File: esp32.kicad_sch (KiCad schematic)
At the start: 22 parts, among them IC1 ESP32-S3-MINI-1U-N8, IC2 CP2102N-A02-GQFN24, J4 USB_C_Receptacle_USB2.0, Q6 NPN, Q7 NPN, SW3 SW_Push, U15 USBLC6-2SC6

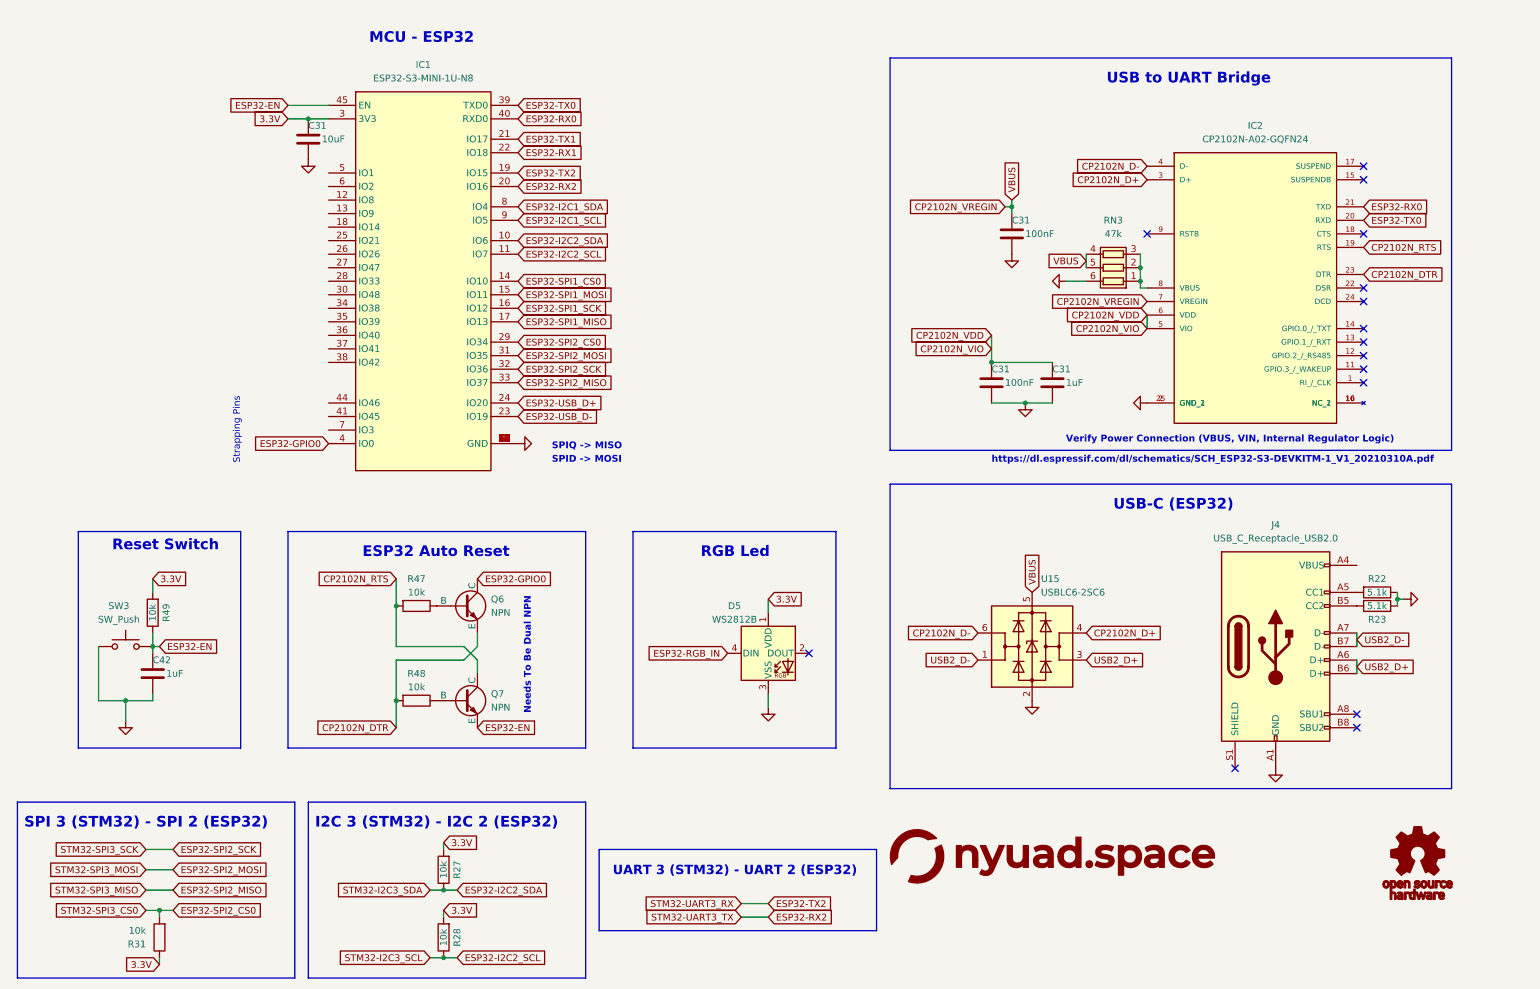
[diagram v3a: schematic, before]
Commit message: Added INA219
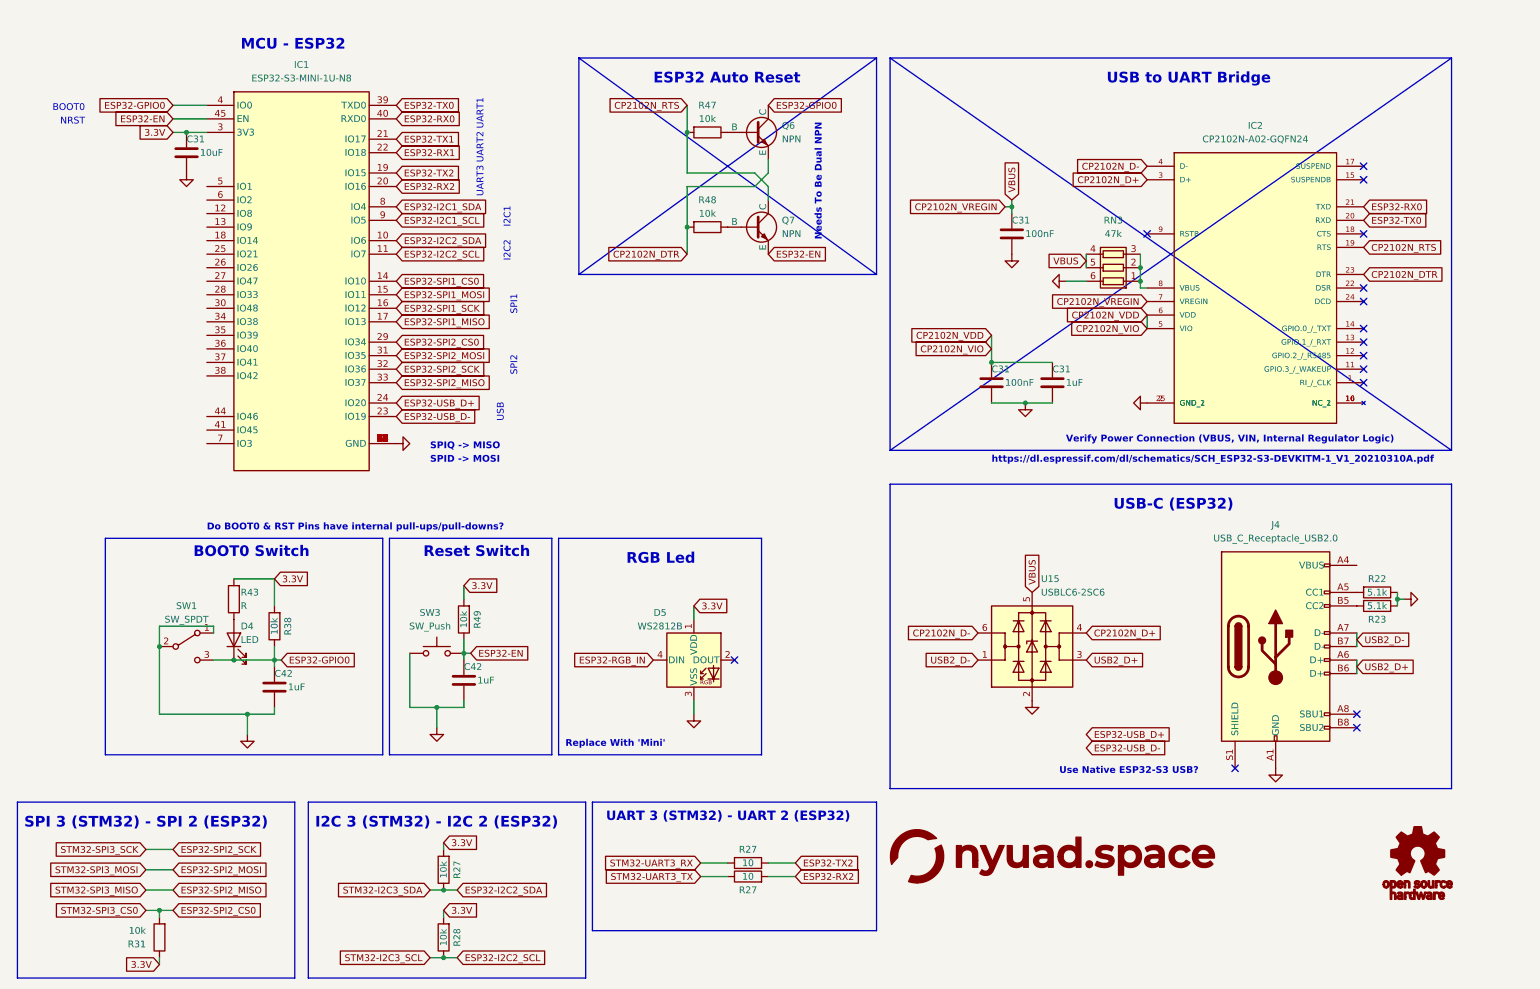
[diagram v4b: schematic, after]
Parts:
- added C42: 1uF, Capacitor_SMD:C_0201_0603Metric, symbol Device:C
- added D4: LED, symbol Device:LED
- added R27 (x2): 10, Resistor_SMD:R_0201_0603Metric, symbol Device:R
- added R38: 10k, symbol Device:R
- added R43: R, symbol Device:R
- added SW1: SW_SPDT, symbol Switch:SW_SPDT
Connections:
- net 3.3V: now also R38.2, R43.2
- net ESP32-GPIO0: now also C42.1, D4.1 (K), R38.1, SW1.3 (C)
- net ESP32-RX2: now also R27.2
- net ESP32-TX2: now also R27.2
- net GND: now also C42.2, SW1.1 (A), SW1.2 (B)
- new net: D4.2 (A), R43.1
- new net STM32-UART3_RX: R27.1
- new net STM32-UART3_TX: R27.1
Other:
- note added: "BOOT0"
- note added: "BOOT0 Switch"
- note added: "Do BOOT0 & RST Pins have internal pull-ups/pull-downs?"
- note added: "I2C1"
- note added: "I2C2"
- note added: "NRST"
- note added: "Replace With 'Mini'"
- note added: "SPI1"
- note added: "SPI2"
- note added: "UART1"
- note added: "UART2"
- note added: "UART3"
- note added: "USB"
- note added: "Use Native ESP32-S3 USB?"
- note removed: "Strapping Pins"
- moved on the sheet: C31, C42, D5, IC1, Q6, Q7, R47, R48, R49, SW3

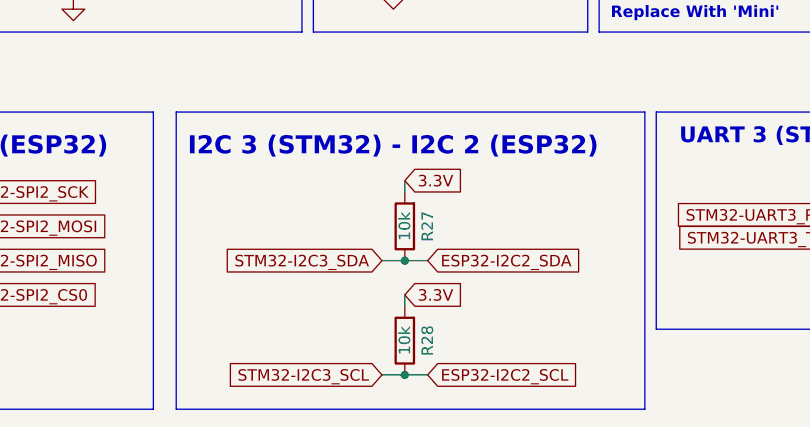
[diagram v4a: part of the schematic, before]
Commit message: Added connectors
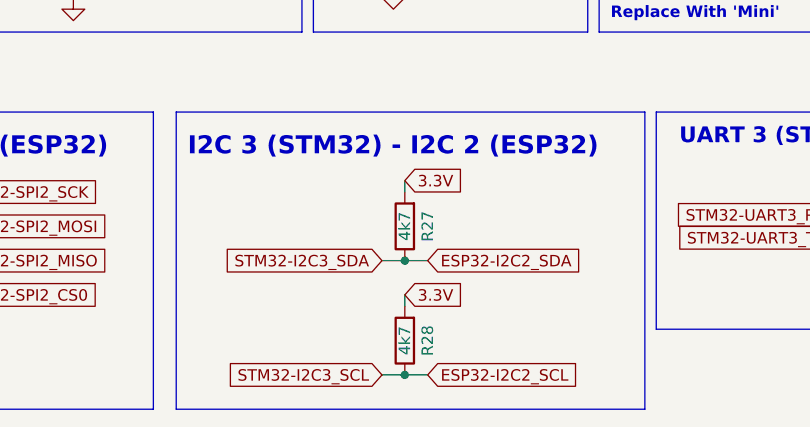
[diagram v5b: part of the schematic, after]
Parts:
- R27, R28: value 10k -> 4k7
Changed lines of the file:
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@@
       (effects (font (size 1.27 1.27)))
     )
-    (property "Value" "10k" (at 93.98 175.26 90)
+    (property "Value" "4k7" (at 93.98 175.26 90)
       (effects (font (size 1.27 1.27)))
     )
@@
       (effects (font (size 1.27 1.27)))
     )
-    (property "Value" "10k" (at 93.98 187.96 90)
+    (property "Value" "4k7" (at 93.98 187.96 90)
       (effects (font (size 1.27 1.27)))
     )
@@
   )
   (symbol (lib_id "power:GND") (at 85.09 95.25 90) (unit 1)
-    (in_bom yes) (on_board yes) (dnp no) (fields_autoplaced)
+    (in_bom yes) (on_board yes) (dnp no)
     (property "Reference" "#PWR043" (at 91.44 95.25 0)
       (effects (font (size 1.27 1.27)) hide)

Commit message: updated footprint library
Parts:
- C31: footprint Capacitor_SMD:C_0201_0603Metric -> Capacitor_SMD:C_0402_1005Metric
- C31: footprint Capacitor_SMD:C_0201_0603Metric -> Capacitor_SMD:C_0603_1608Metric
- R22, R23, R27, R31: footprint Resistor_SMD:R_0201_0603Metric -> Resistor_SMD:R_0402_1005Metric
- R38, R43, R47, R48, R49: footprint (none) -> Resistor_SMD:R_0402_1005Metric
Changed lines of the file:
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@@
       (effects (font (size 1.27 1.27)) (justify left))
     )
-    (property "Footprint" "Capacitor_SMD:C_0201_0603Metric" (at 197.8152 87.63 0)
+    (property "Footprint" "Capacitor_SMD:C_0402_1005Metric" (at 197.8152 87.63 0)
       (effects (font (size 1.27 1.27)) hide)
     )
@@
       (effects (font (size 1.27 1.27)))
     )
-    (property "Footprint" "" (at 143.51 35.052 90)
+    (property "Footprint" "Resistor_SMD:R_0402_1005Metric" (at 143.51 35.052 90)
       (effects (font (size 1.27 1.27)) hide)
     )
@@
       (effects (font (size 1.27 1.27)) (justify right))
     )
-    (property "Footprint" "" (at 56.388 124.46 90)
+    (property "Footprint" "Resistor_SMD:R_0402_1005Metric" (at 56.388 124.46 90)
       (effects (font (size 1.27 1.27)) hide)
     )
@@
       (effects (font (size 1.27 1.27)))
     )
-    (property "Footprint" "Resistor_SMD:R_0201_0603Metric" (at 269.24 121.412 90)
+    (property "Footprint" "Resistor_SMD:R_0402_1005Metric" (at 269.24 121.412 90)
       (effects (font (size 1.27 1.27)) hide)
     )
@@
       (effects (font (size 1.27 1.27)) (justify left))
     )
-    (property "Footprint" "Resistor_SMD:R_0201_0603Metric" (at 42.418 187.96 90)
+    (property "Footprint" "Resistor_SMD:R_0402_1005Metric" (at 42.418 187.96 90)
       (effects (font (size 1.27 1.27)) hide)
     )
@@
       (effects (font (size 1.27 1.27)))
     )
-    (property "Footprint" "" (at 143.51 52.832 90)
+    (property "Footprint" "Resistor_SMD:R_0402_1005Metric" (at 143.51 52.832 90)
       (effects (font (size 1.27 1.27)) hide)
     )
@@
       (effects (font (size 1.27 1.27)))
     )
-    (property "Footprint" "Resistor_SMD:R_0201_0603Metric" (at 151.13 178.308 90)
+    (property "Footprint" "Resistor_SMD:R_0402_1005Metric" (at 151.13 178.308 90)
       (effects (font (size 1.27 1.27)) hide)
     )
@@
       (effects (font (size 1.27 1.27)) (justify left))
     )
-    (property "Footprint" "Capacitor_SMD:C_0201_0603Metric" (at 46.6852 44.45 0)
+    (property "Footprint" "Capacitor_SMD:C_0603_1608Metric" (at 46.6852 44.45 0)
       (effects (font (size 1.27 1.27)) hide)
     )
@@
       (effects (font (size 1.27 1.27)) (justify left))
     )
-    (property "Footprint" "Capacitor_SMD:C_0201_0603Metric" (at 201.6252 59.69 0)
+    (property "Footprint" "Capacitor_SMD:C_0402_1005Metric" (at 201.6252 59.69 0)
       (effects (font (size 1.27 1.27)) hide)
     )
@@
       (effects (font (size 1.27 1.27)))
     )
-    (property "Footprint" "Resistor_SMD:R_0201_0603Metric" (at 151.13 175.768 90)
+    (property "Footprint" "Resistor_SMD:R_0402_1005Metric" (at 151.13 175.768 90)
       (effects (font (size 1.27 1.27)) hide)
     )
@@
       (effects (font (size 1.27 1.27)))
     )
-    (property "Footprint" "" (at 99.568 128.27 90)
+    (property "Footprint" "Resistor_SMD:R_0402_1005Metric" (at 99.568 128.27 90)
       (effects (font (size 1.27 1.27)) hide)
     )
@@
       (effects (font (size 1.27 1.27)))
     )
-    (property "Footprint" "Resistor_SMD:R_0201_0603Metric" (at 269.24 127.508 90)
+    (property "Footprint" "Resistor_SMD:R_0402_1005Metric" (at 269.24 127.508 90)
       (effects (font (size 1.27 1.27)) hide)
     )
@@
       (effects (font (size 1.27 1.27)))
     )
-    (property "Footprint" "" (at 64.008 129.54 90)
-      (effects (font (size 1.27 1.27)) hide)
-    )
+    (property "Footprint" "Resistor_SMD:R_0402_1005Metric" (at 64.008 129.54 90)
+      (effects (font (size 1.27 1.27)) hide)
+    )

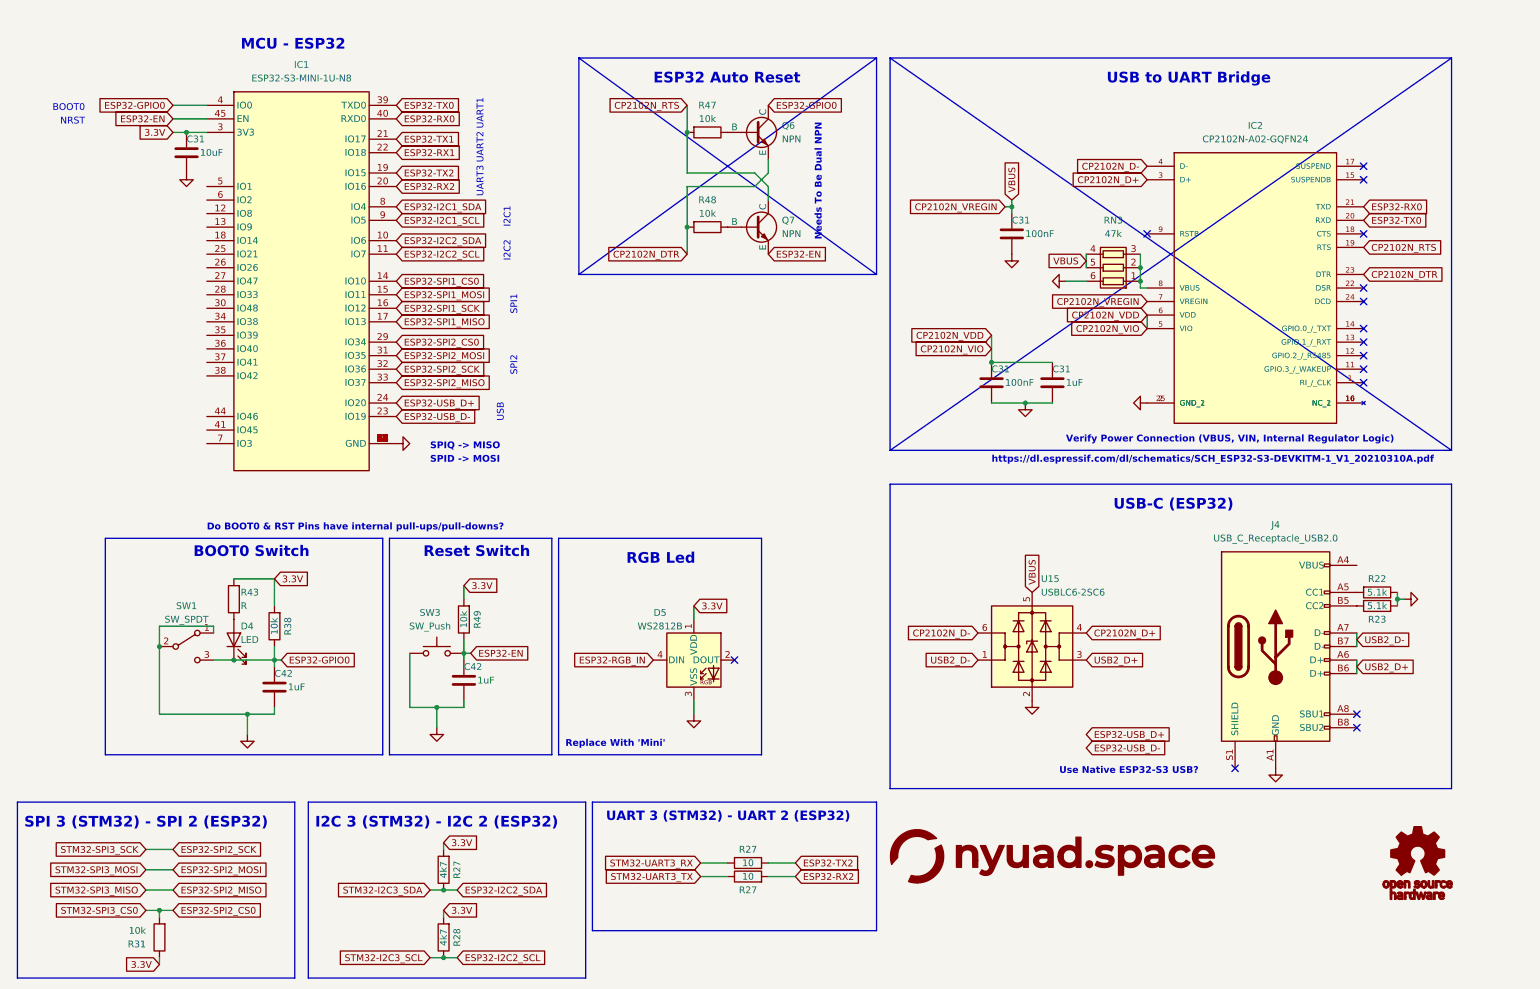
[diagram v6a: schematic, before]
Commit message: Updated symbol footprints
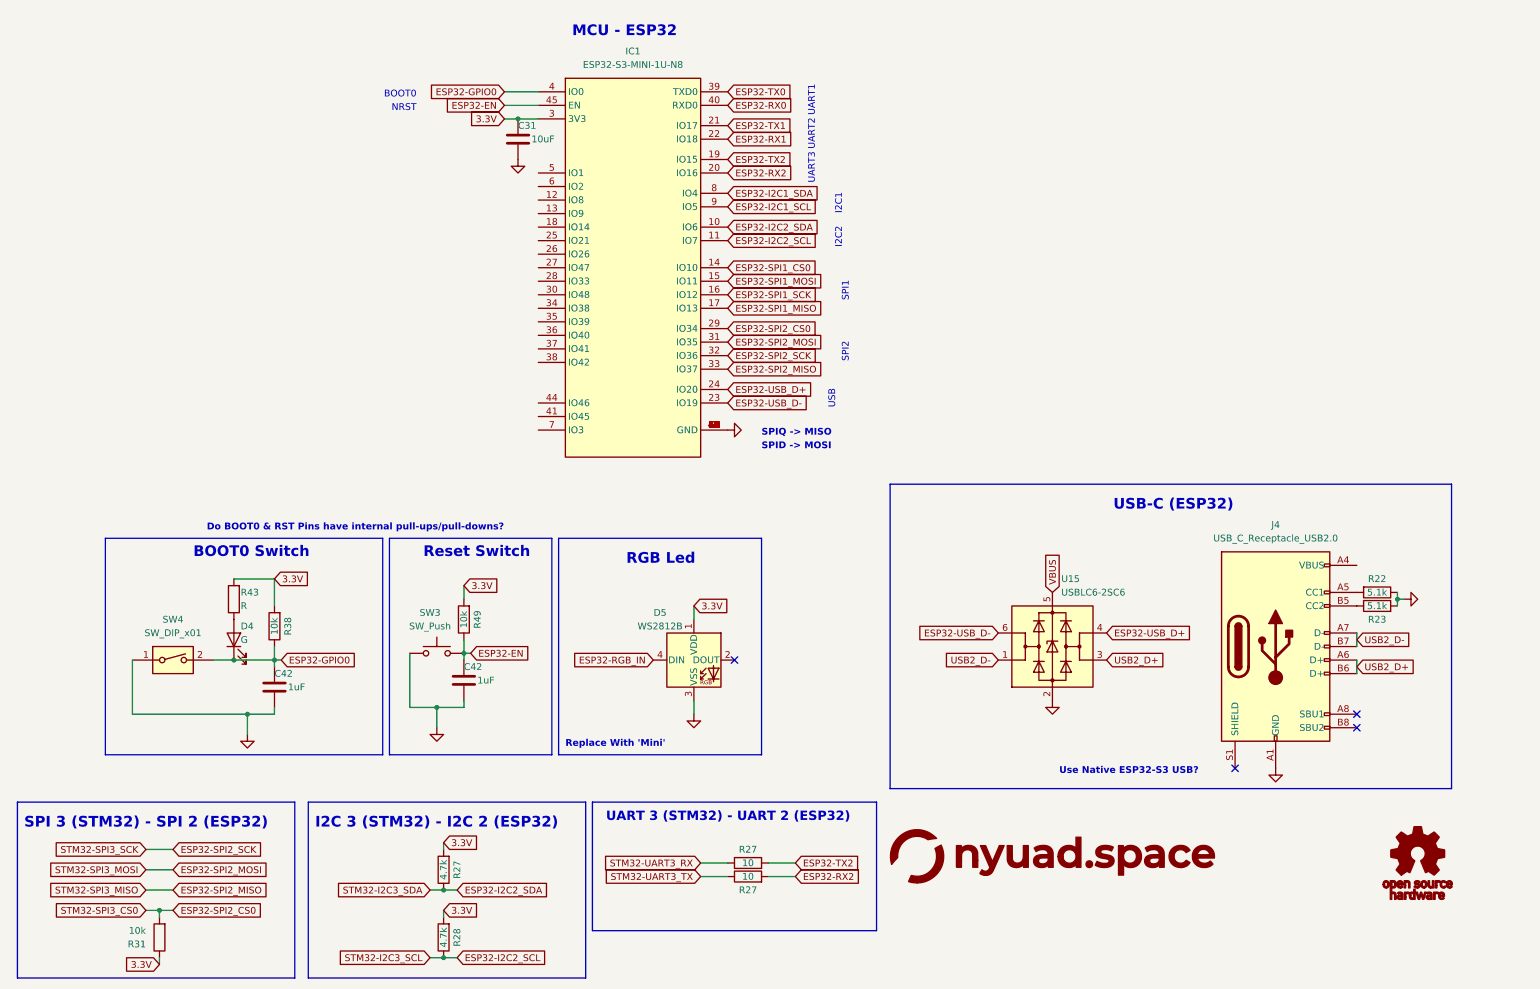
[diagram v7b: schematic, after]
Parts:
- removed C31 (x2): 100nF, Capacitor_SMD:C_0402_1005Metric, symbol Device:C
- removed C31: 1uF, Capacitor_SMD:C_0201_0603Metric, symbol Device:C
- removed IC2: CP2102N-A02-GQFN24, QFN50P400X400X80-25N, symbol CP2102N-A02-GQFN24:CP2102N-A02-GQFN24
- removed Q6, Q7: NPN, symbol Simulation_SPICE:NPN
- removed R47, R48: 10k, Resistor_SMD:R_0402_1005Metric, symbol Device:R
- removed RN3: 47k, symbol Device:R_Pack03
- removed SW1: SW_SPDT, symbol Switch:SW_SPDT
- added SW4: SW_DIP_x01, symbol Switch:SW_DIP_x01
- C42: footprint Capacitor_SMD:C_0201_0603Metric -> Capacitor_SMD:C_0603_1608Metric
- D4: value LED -> G; footprint (none) -> LED_SMD:LED_0603_1608Metric
- J4: footprint (none) -> Connector_USB:USB_C_Receptacle_GCT_USB4105-xx-A_16P_TopMnt_Horizontal
- R22, R23, R31, R38, R43, R49: footprint Resistor_SMD:R_0402_1005Metric -> Resistor_SMD:R_0603_1608Metric
- R27, R28: value 4k7 -> 4.7k; footprint Resistor_SMD:R_0201_0603Metric -> Resistor_SMD:R_0402_1005Metric
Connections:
- net CP2102N_D+ is gone; now on net ESP32-USB_D+: U15.4 (I/O2)
- net CP2102N_D- is gone; now on net ESP32-USB_D-: U15.6 (I/O1)
- net ESP32-GPIO0: now also SW4.2
- net GND: now also SW4.1
- net CP2102N_VREGIN renamed VBUS
- no-connect marks 15 -> 4
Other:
- note removed: "ESP32 Auto Reset"
- note removed: "Needs To Be Dual NPN"
- note removed: "USB to UART Bridge"
- note removed: "Verify Power Connection (VBUS, VIN, Internal Regulator Logic)"
- note removed: "https://dl.espressif.com/dl/schematics/SCH_ESP32-S3-DEVKITM-1_V1_20210310A.pdf"
- moved on the sheet: C31, IC1, U15

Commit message: updated schematic
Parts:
- removed SW3: SW_Push, symbol Switch:SW_Push
- removed SW4: SW_DIP_x01, symbol Switch:SW_DIP_x01
- added SW4: PTS526_SM08_SMTR2_LFS, PTS526_SM08_SMTR2_LFS:SW_PTS526_SM08_SMTR2_LFS, symbol PTS526_SM08_SMTR2_LFS:PTS526_SM08_SMTR2_LFS
- added SW?: TDD01H0SB1R, TDD01H0SB1R:SOT175P420X230-3N, symbol TDD01H0SB1R:TDD01H0SB1R
- IC?: renamed from IC1; footprint ESP32S3MINI1UN8 -> ESP32S3MINI1UN8:ESP32S3MINI1UN8
- renumbered C42 to C?, C31 to C?, D5 to D?, D4 to D?, J4 to J?, R38 to R14, R49 to R17, R27 to R?, R43 to R?, R22 to R?, R28 to R?, R31 to R?, R23 to R?, U15 to U?
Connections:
- net ESP32-EN: now also SW4.3, SW4.4
- net ESP32-GPIO0: now also SW?.1
- net GND: now also SW4.1, SW4.2, SW?.3 (C)
- no-connect marks 4 -> 5
